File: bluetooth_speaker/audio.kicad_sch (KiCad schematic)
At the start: 4 parts, among them U1 MAX98357A

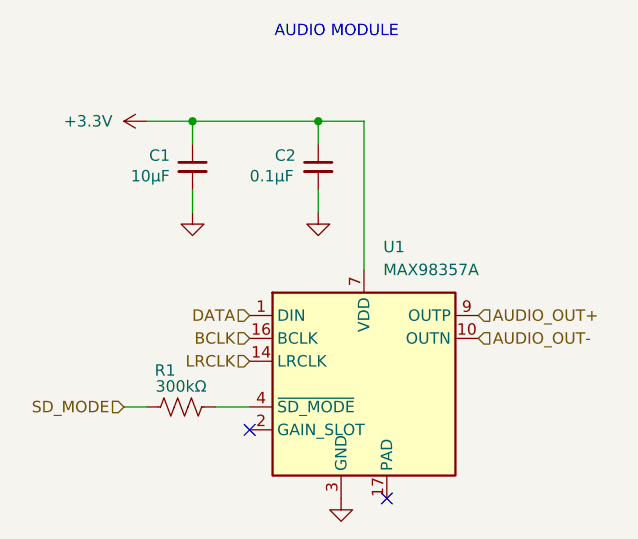
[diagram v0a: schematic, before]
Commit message: adding few footprints
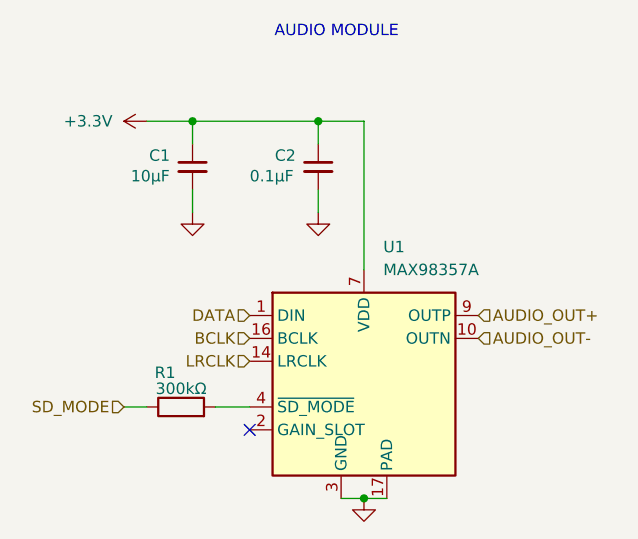
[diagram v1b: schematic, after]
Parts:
- removed R1: 300kΩ, symbol Device:R_US
- added R1: 300kΩ, Resistor_SMD:R_0603_1608Metric_Pad0.98x0.95mm_HandSolder, symbol Device:R
- C1, C2: footprint (none) -> Capacitor_SMD:C_0603_1608Metric_Pad1.08x0.95mm_HandSolder
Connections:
- net GND: now also U1.17 (PAD)
- net SD_MODE: now also R1.1
- net at U1.4 (~{SD_MODE}): now also R1.2
- no-connect marks 2 -> 1
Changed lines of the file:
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@@
+	)
+	(junction
+		(at 87.63 85.09)
+		(diameter 0)
+		(color 0 0 0 0)
 	)
 	(junction
@@
 	)
 	(no_connect
-		(at 90.17 85.09)
-	)
-	(no_connect
 		(at 74.93 77.47)
 	)
 	(wire
 		(pts
+			(xy 85.09 85.09) (xy 87.63 85.09)
+		)
+		(stroke
+			(width 0)
+			(type default)
+		)
+	)
+	(wire
+		(pts
 			(xy 68.58 43.18) (xy 68.58 45.72)
 		)
@@
 		(pts
 			(xy 71.12 74.93) (xy 74.93 74.93)
+		)
+		(stroke
+			(width 0)
+			(type default)
+		)
+	)
+	(wire
+		(pts
+			(xy 87.63 85.09) (xy 90.17 85.09)
 		)
 		(stroke
@@
 			)
 		)
-		(property "Footprint" ""
+		(property "Footprint" "Capacitor_SMD:C_0603_1608Metric_Pad1.08x0.95mm_HandSolder"
 			(at 82.55 48.26 0)
 			(effects
@@
 	)
 	(symbol
+		(lib_id "Device:R")
+		(at 67.31 74.93 90)
+		(unit 1)
+		(exclude_from_sim no)
+		(in_bom yes)
+		(on_board yes)
+		(dnp no)
+		(property "Reference" "R1"
+			(at 65.532 71.12 90)
+			(effects
+				(font
+					(size 1.27 1.27)
+				)
+			)
+		)
+		(property "Value" "300kΩ"
+			(at 67.31 72.898 90)
+			(effects
+				(font
+					(size 1.27 1.27)
+				)
+			)
+		)
+		(property "Footprint" "Resistor_SMD:R_0603_1608Metric_Pad0.98x0.95mm_HandSolder"
+			(at 67.31 76.708 90)
+			(effects
+				(font
+					(size 1.27 1.27)
+				)
+				(hide yes)
+			)
+		)
+		(property "Datasheet" "~"
+			(at 67.31 74.93 0)
+			(effects
+				(font
+					(size 1.27 1.27)
+				)
+				(hide yes)
+			)
+		)
+		(property "Description" "Resistor"
+			(at 67.31 74.93 0)
+			(effects
+				(font
+					(size 1.27 1.27)
+				)
+				(hide yes)
+			)
+		)
+		(pin "1"
+		)
+		(pin "2"
+		)
+		(instances
+			(project "bluetooth_speaker"
+				(path "/13ff5fb5-140a-4554-92d9-4ae3849ea082/a18431ea-692e-404c-95d5-0160882d1cfb"
+					(reference "R1")
+					(unit 1)
+				)
+			)
+		)
+	)
+	(symbol
 		(lib_id "Audio:MAX98357A")
 		(at 87.63 72.39 0)
@@
 			)
 		)
-		(property "Footprint" ""
+		(property "Footprint" "Capacitor_SMD:C_0603_1608Metric_Pad1.08x0.95mm_HandSolder"
 			(at 68.58 48.26 0)
 			(effects
@@
 	)
 	(symbol
-		(lib_id "Device:R_US")
-		(at 67.31 74.93 90)
-		(unit 1)
-		(exclude_from_sim no)
-		(in_bom yes)
-		(on_board yes)
-		(dnp no)
-		(property "Reference" "R1"
-			(at 65.532 70.866 90)
-			(effects
-				(font
-					(size 1.27 1.27)
-				)
-			)
-		)
-		(property "Value" "300kΩ"
-			(at 67.31 72.644 90)
-			(effects
-				(font
-					(size 1.27 1.27)
-				)
-			)
-		)
-		(property "Footprint" ""
-			(at 67.564 73.914 90)
-			(effects
-				(font
-					(size 1.27 1.27)
-				)
-				(hide yes)
-			)
-		)
-		(property "Datasheet" "~"
-			(at 67.31 74.93 0)
-			(effects
-				(font
-					(size 1.27 1.27)
-				)
-				(hide yes)
-			)
-		)
-		(property "Description" "Resistor, US symbol"
-			(at 67.31 74.93 0)
-			(effects
-				(font
-					(size 1.27 1.27)
-				)
-				(hide yes)
-			)
-		)
-		(pin "1"
-		)
-		(pin "2"
-		)
-		(instances
-			(project "bluetooth_speaker"
-				(path "/13ff5fb5-140a-4554-92d9-4ae3849ea082/a18431ea-692e-404c-95d5-0160882d1cfb"
-					(reference "R1")
-					(unit 1)
-				)
-			)
-		)
-	)
-	(symbol
 		(lib_id "power:GND")
-		(at 85.09 85.09 0)
+		(at 87.63 85.09 0)
 		(unit 1)
 		(exclude_from_sim no)
@@
 		(fields_autoplaced yes)
 		(property "Reference" "#PWR01"
-			(at 85.09 91.44 0)
+			(at 87.63 91.44 0)
 			(effects
 				(font
@@
 		)
 		(property "Value" "GND"
-			(at 85.09 90.17 0)
+			(at 87.63 90.17 0)
 			(effects
 				(font
@@
 		)
 		(property "Footprint" ""
-			(at 85.09 85.09 0)
+			(at 87.63 85.09 0)
 			(effects
 				(font
@@
 		)
 		(property "Datasheet" ""
-			(at 85.09 85.09 0)
+			(at 87.63 85.09 0)
 			(effects
 				(font
@@
 		)
 		(property "Description" "Power symbol creates a global label with name \"GND\" , ground"
-			(at 85.09 85.09 0)
-			(effects
-				(font
+			(at 87.63 85.09 0)
+			(effects
+				(font

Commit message: Completed the PCB design
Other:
- company: (none) -> Politechnika Poznańska
- title: (none) -> bluetooth speaker
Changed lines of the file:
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@@
 	(generator_version "9.0")
 	(paper "A4")
+	(title_block
+		(title "bluetooth speaker")
+		(date "2026-01-05")
+		(rev "1.0")
+		(company "Politechnika Poznańska")
+	)
 	(text "AUDIO MODULE"
 		(exclude_from_sim no)

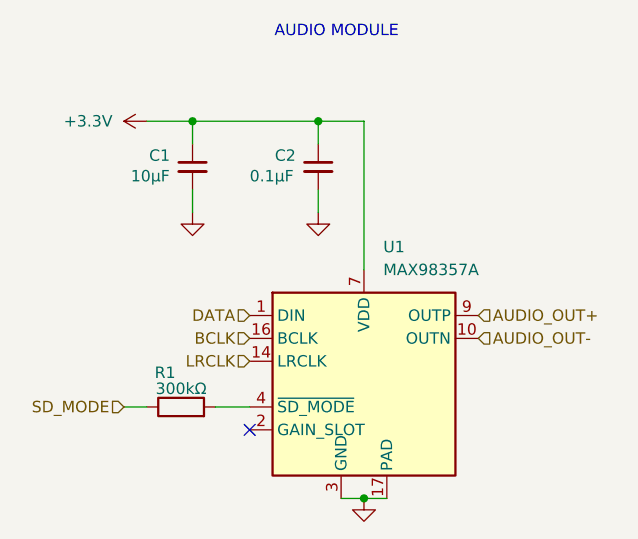
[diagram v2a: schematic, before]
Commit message: Exchanged CP2102N to CP2102C due to discontinuation
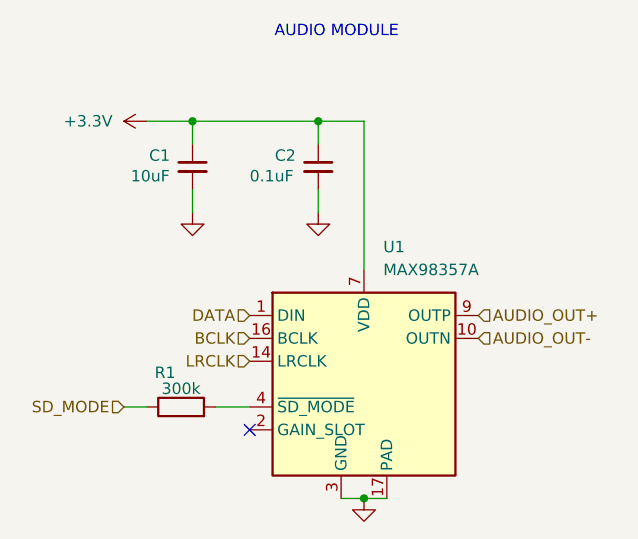
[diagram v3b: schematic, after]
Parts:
- C1: value 10µF -> 10uF
- C2: value 0.1µF -> 0.1uF
- R1: value 300kΩ -> 300k
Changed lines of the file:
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@@
 			)
 		)
-		(property "Value" "0.1µF"
+		(property "Value" "0.1uF"
 			(at 74.93 49.276 0)
 			(effects
@@
 			)
 		)
-		(property "Value" "300kΩ"
+		(property "Value" "300k"
 			(at 67.31 72.898 90)
 			(effects
@@
 			)
 		)
-		(property "Value" "10µF"
+		(property "Value" "10uF"
 			(at 61.722 49.276 0)
 			(effects
